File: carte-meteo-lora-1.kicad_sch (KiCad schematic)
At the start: 95 parts, among them J1 Conn_01x04, J2 USB_C_Receptacle_USB2.0_14P, J4 Conn_01x04_Pin, Q1 Q_NMOS, Q2 Q_NMOS, SW1 SW_SPST, U1 MS5607-02BA, U2 BQ77905, U3 HS96L03W2C03, U4 ESP32-S3FN8, U5 LDL212PV33R, U6 ESP32-C5, Y1 48M

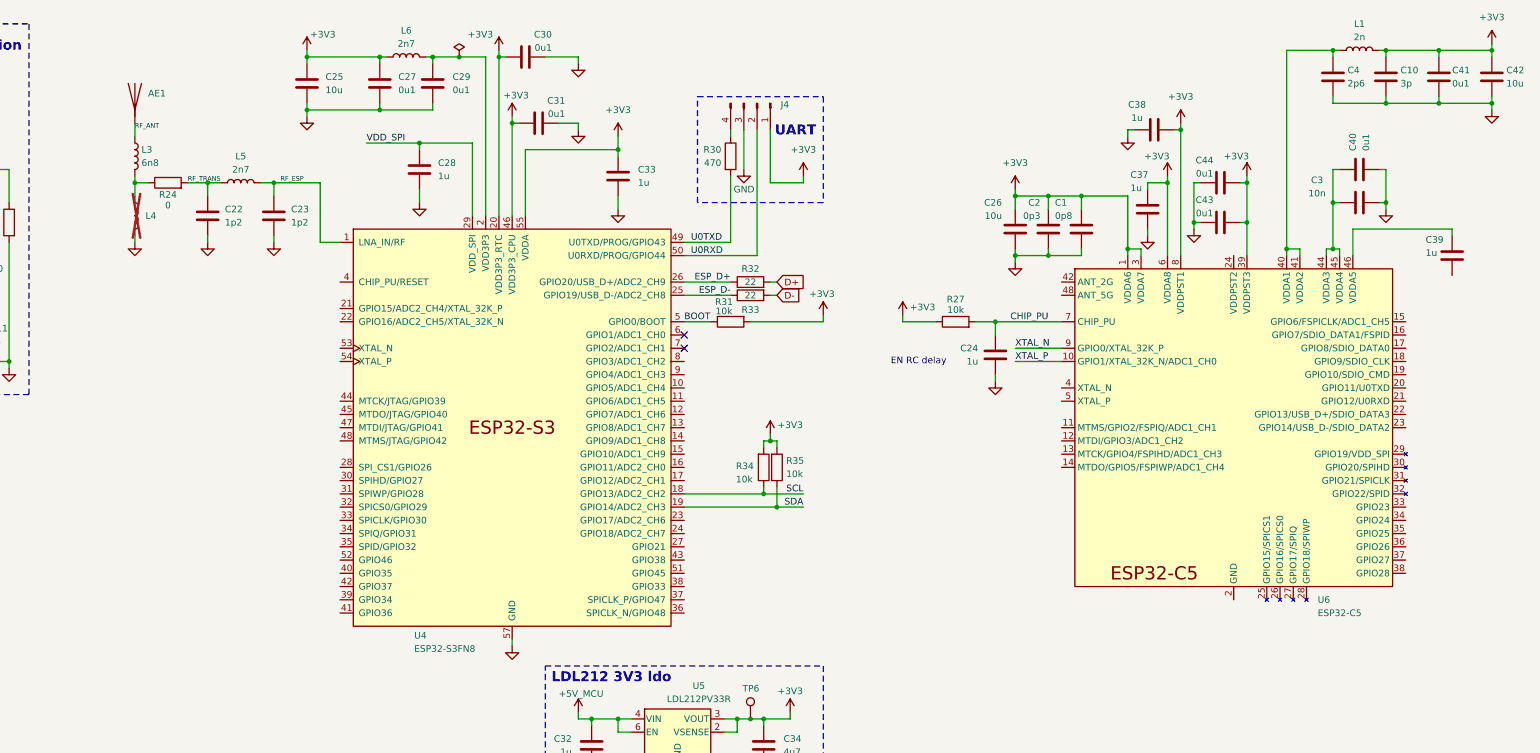
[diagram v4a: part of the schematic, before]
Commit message: schem: replace esp32-s3 with esp32-c5
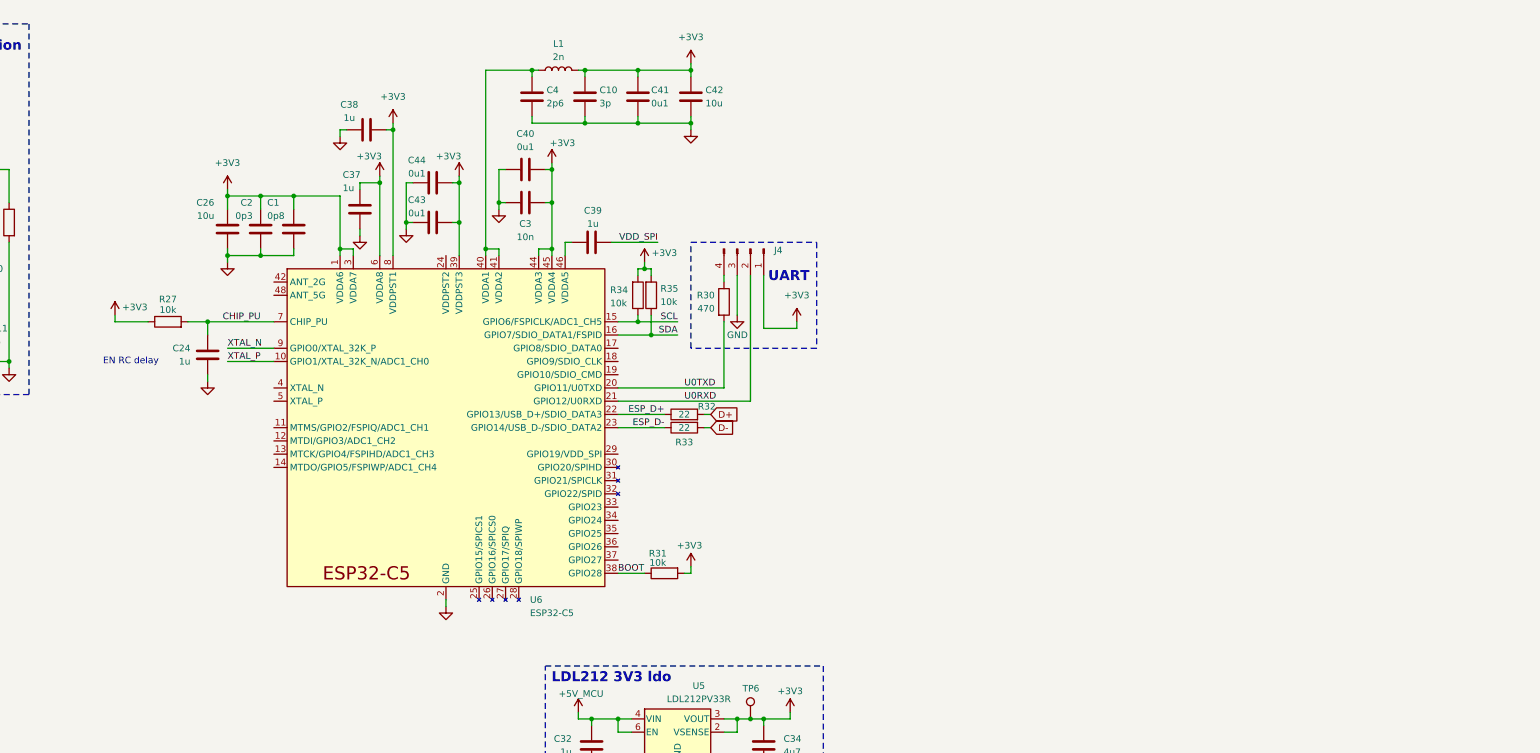
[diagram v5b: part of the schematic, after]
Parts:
- removed AE1: Antenna, RF_Antenna:Johanson_2450AT18x100, symbol Device:Antenna
- removed C22, C23: 1p2, Capacitor_SMD:C_0402_1005Metric, symbol Device:C
- removed C25: 10u, Capacitor_SMD:C_0402_1005Metric, symbol Device:C
- removed C27, C29, C30, C31: 0u1, Capacitor_SMD:C_0402_1005Metric, symbol Device:C
- removed C28, C33: 1u, Capacitor_SMD:C_0402_1005Metric, symbol Device:C
- removed L3: 6n8, Inductor_SMD:L_0402_1005Metric, symbol Device:L
- removed L4: L, Inductor_SMD:L_0402_1005Metric, symbol Device:L
- removed L5, L6: 2n7, Inductor_SMD:L_0402_1005Metric, symbol Device:L
- removed R24: 0, Resistor_SMD:R_0402_1005Metric, symbol Device:R
- removed U4: ESP32-S3FN8, Package_DFN_QFN:QFN-56-1EP_7x7mm_P0.4mm_EP4x4mm_ThermalVias, symbol PCM_Espressif:ESP32-S3
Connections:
- net +3V3: now also C3.1, C40.1, U6.44 (VDDA3), U6.45 (VDDA4)
- net BOOT: now also U6.38 (GPIO28)
- net ESP_D+: now also U6.22 (GPIO13/USB_D+/SDIO_DATA3)
- net ESP_D-: now also U6.23 (GPIO14/USB_D-/SDIO_DATA2)
- net SCL: now also U6.15 (GPIO6/FSPICLK/ADC1_CH5)
- net SDA: now also U6.16 (GPIO7/SDIO_DATA1/FSPID)
- net U0RXD: now also U6.21 (GPIO12/U0RXD)
- net U0TXD: now also U6.20 (GPIO11/U0TXD)
- net VDD_SPI: now also C39.2
- net at U6.46 (VDDA5): now also C39.1; no longer C39.2
- no-connect marks 5 -> 3
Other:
- moved on the sheet: C1, C2, C24, C26, C3, C37, C38, C39, C40, C43, C44, R27

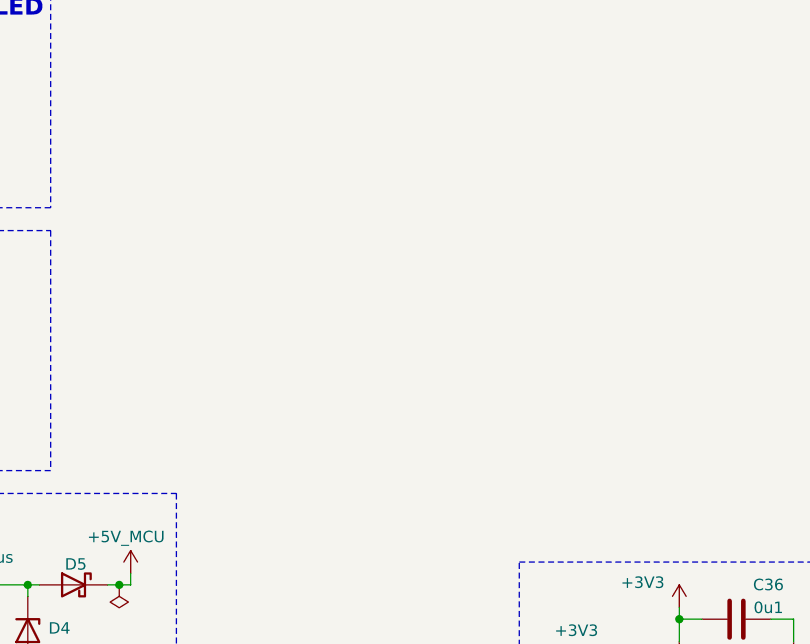
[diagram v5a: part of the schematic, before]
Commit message: schem: add GXHT30 humidity and temperature sensor
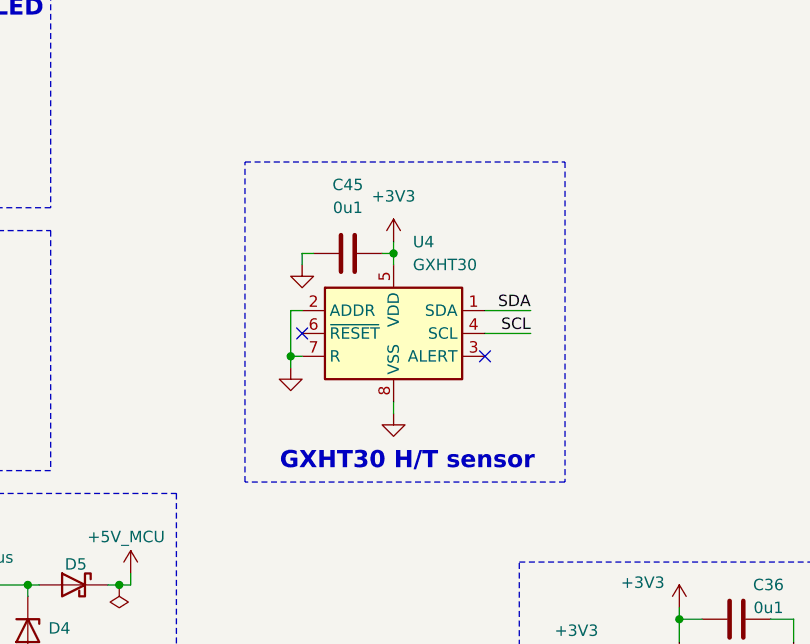
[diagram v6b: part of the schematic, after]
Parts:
- added C45: 0u1, Capacitor_SMD:C_0402_1005Metric, symbol Device:C
- added U4: GXHT30, Sensor_Humidity:Sensirion_DFN-8-1EP_2.5x2.5mm_P0.5mm_EP1.1x1.7mm, symbol Sensor_Humidity:SHT30-DIS
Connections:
- net +3V3: now also C45.2, U4.5 (VDD)
- net GND: now also C45.1, U4.2 (ADDR), U4.7 (R), U4.8 (VSS), U4.9 (VSS)
- net SCL: now also U4.4 (SCL)
- net SDA: now also U4.1 (SDA)
- no-connect marks 3 -> 5
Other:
- note added: "GXHT30 H/T sensor"

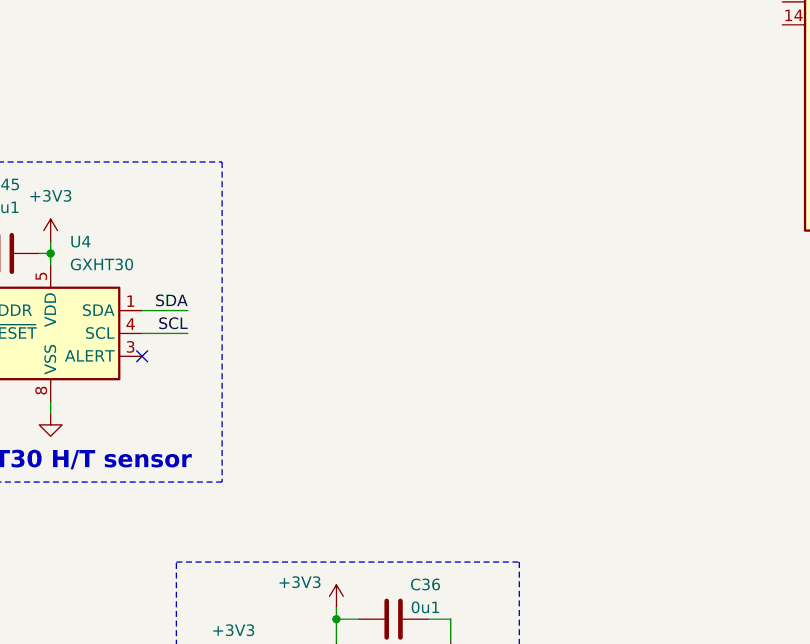
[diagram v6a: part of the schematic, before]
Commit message: schem: add HTU21 humidity and temperature
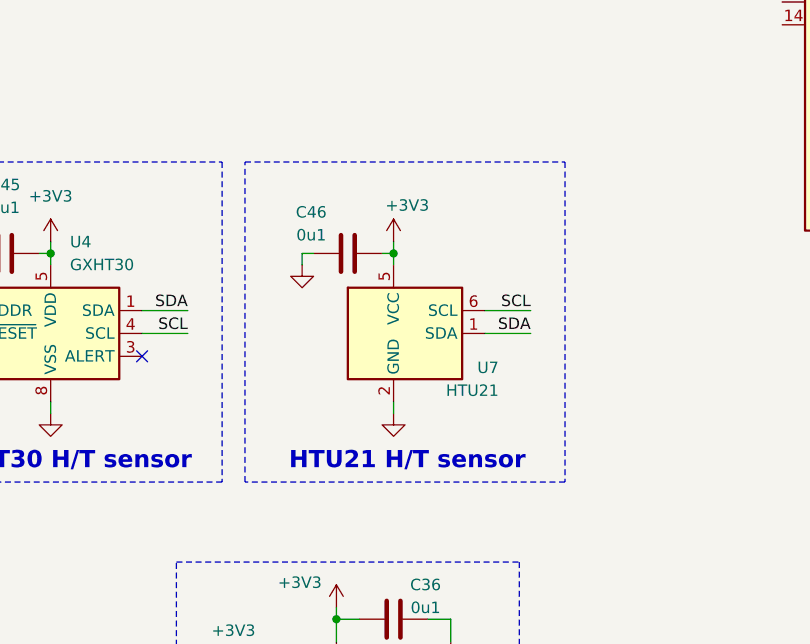
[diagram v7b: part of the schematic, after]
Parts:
- added C46: 0u1, Capacitor_SMD:C_0402_1005Metric, symbol Device:C
- added U7: HTU21, Package_SON:Texas_PWSON-N6, symbol Sensor_Humidity:HDC1080
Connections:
- net +3V3: now also C46.2, U7.5 (VCC)
- net GND: now also C46.1, U7.2 (GND)
- net SCL: now also U7.6 (SCL)
- net SDA: now also U7.1 (SDA)
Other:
- note added: "HTU21 H/T sensor"

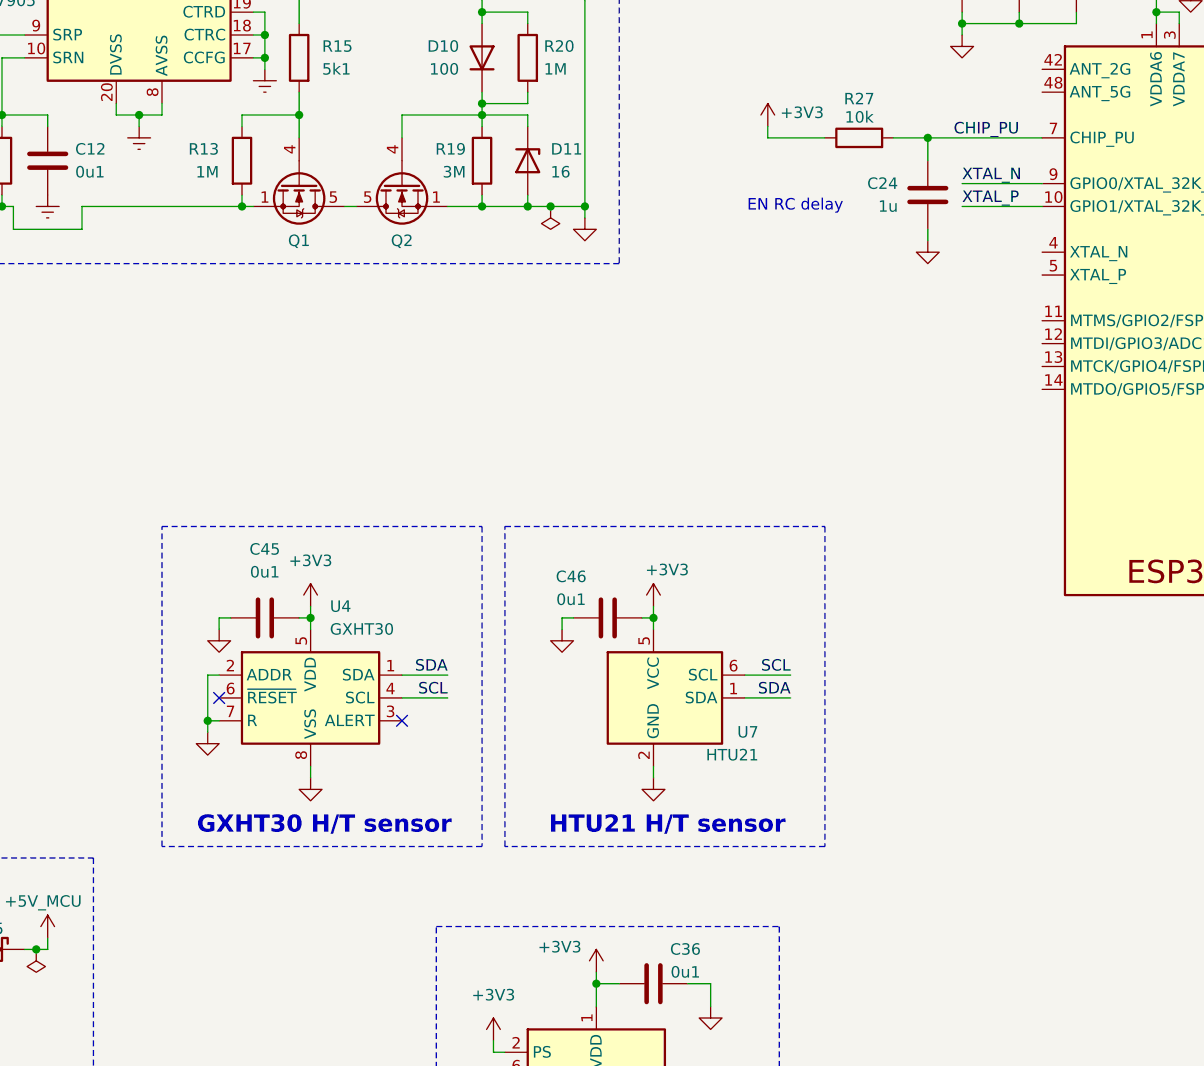
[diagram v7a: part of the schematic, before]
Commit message: schem: add wind and rain connectors
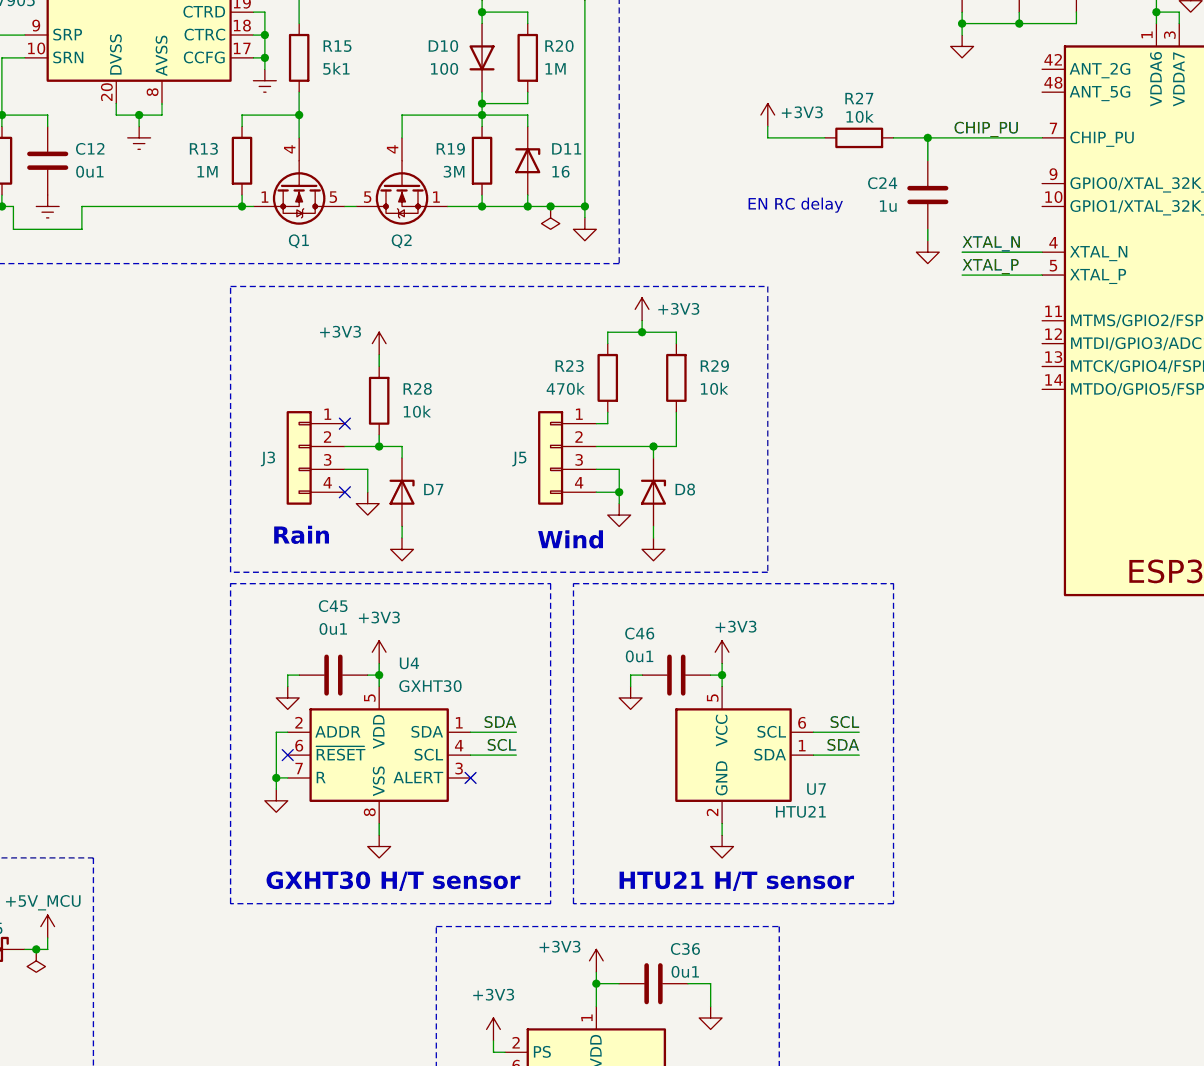
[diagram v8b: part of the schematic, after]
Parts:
- added D7, D8: H5VU10U, GLCS:Diode_DFN1006, symbol GLCS:H5VU10U
- added J3, J5: Conn_01x04, symbol Connector_Generic:Conn_01x04
- added R23: 470k, Resistor_SMD:R_0603_1608Metric, symbol Device:R
- added R28, R29: 10k, Resistor_SMD:R_0402_1005Metric, symbol Device:R
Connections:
- net +3V3: now also R23.1, R28.2, R29.2
- net GND: now also D7.2 (A), D8.2 (A), J3.3 (Pin_3), J5.3 (Pin_3), J5.4 (Pin_4)
- net XTAL_N: now also U6.4 (XTAL_N); no longer U6.9 (GPIO0/XTAL_32K_P)
- net XTAL_P: now also U6.5 (XTAL_P); no longer U6.10 (GPIO1/XTAL_32K_N/ADC1_CH0)
- new net: D7.1 (K), J3.2 (Pin_2), R28.1
- new net: D8.1 (K), J5.2 (Pin_2), R29.1
- new net: J5.1 (Pin_1), R23.2
- no-connect marks 5 -> 7
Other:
- note added: "Rain"
- note added: "Wind"
- moved on the sheet: C45, C46, U4, U7
